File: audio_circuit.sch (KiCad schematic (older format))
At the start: 21 parts

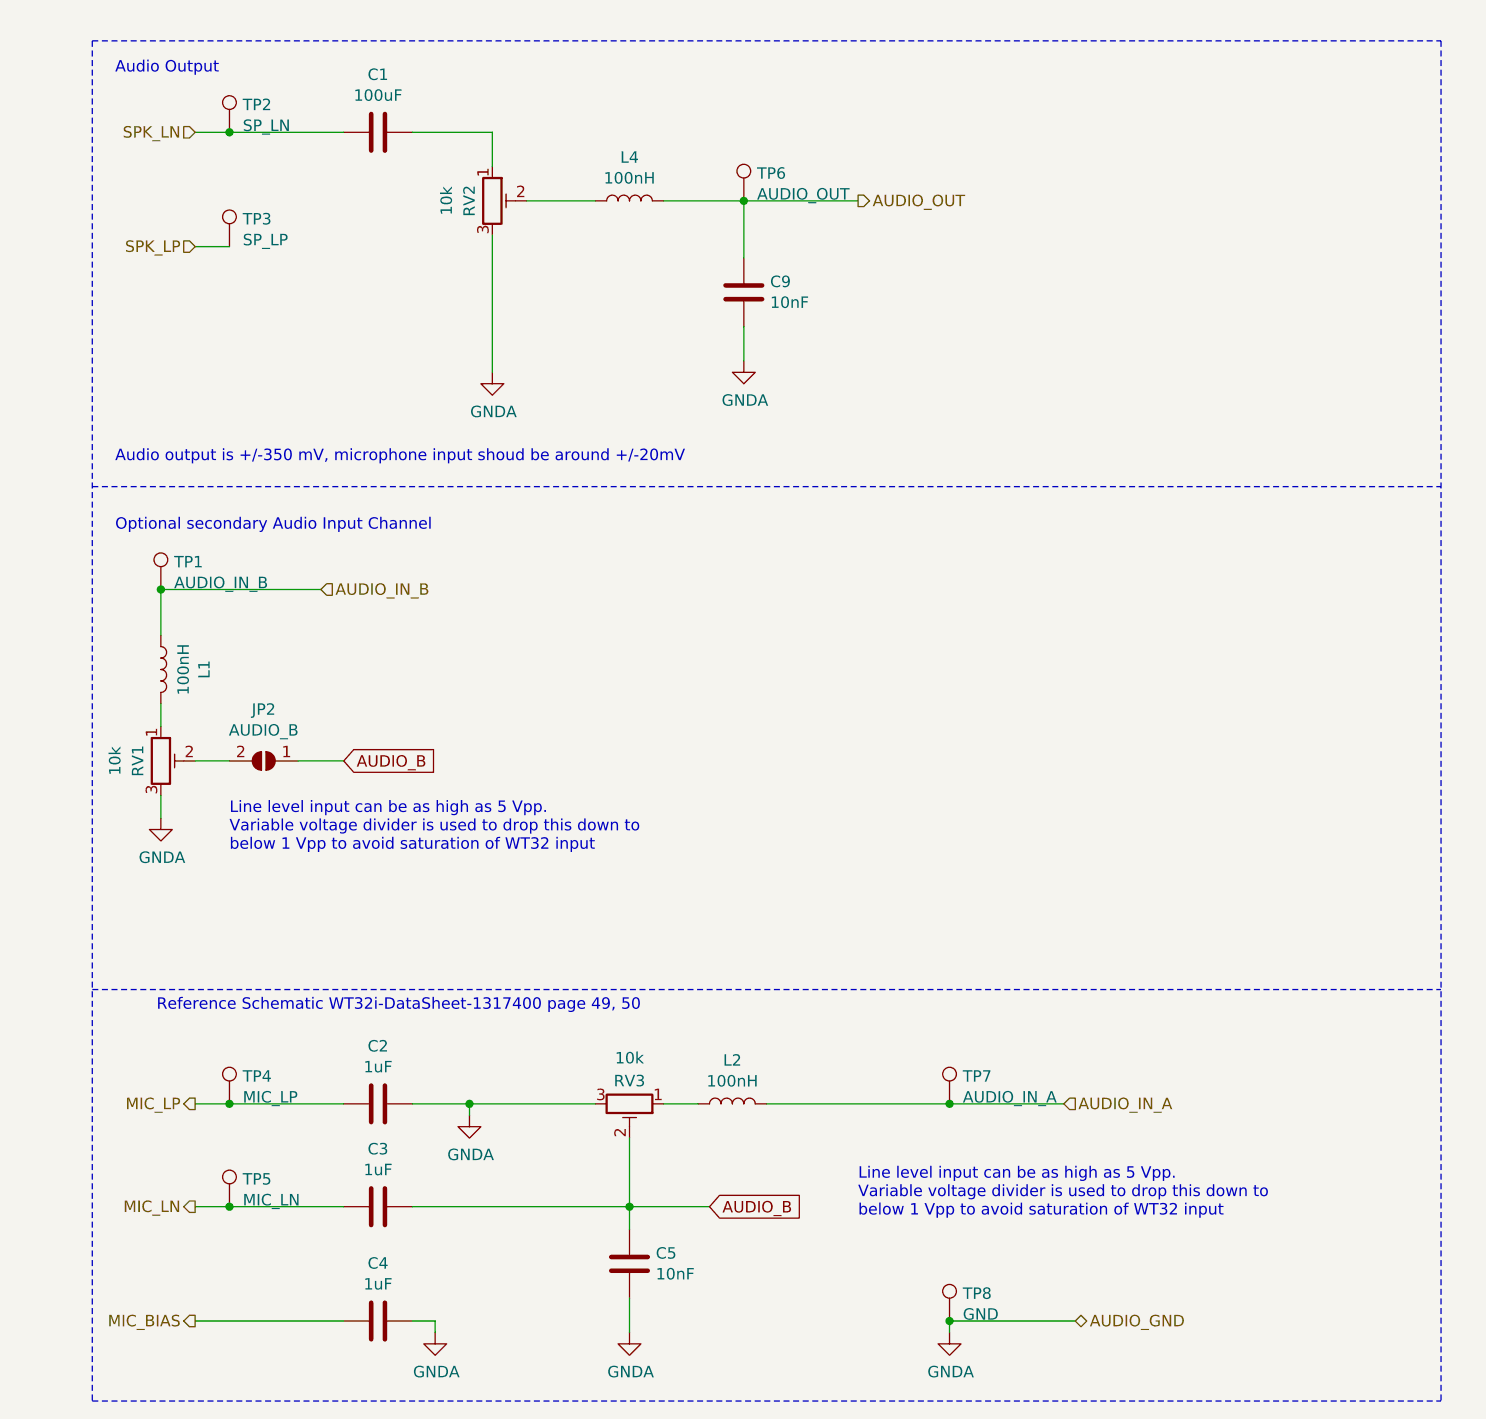
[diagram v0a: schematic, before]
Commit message: Assigned Pins to ESP32 and removed Teensy [#1]
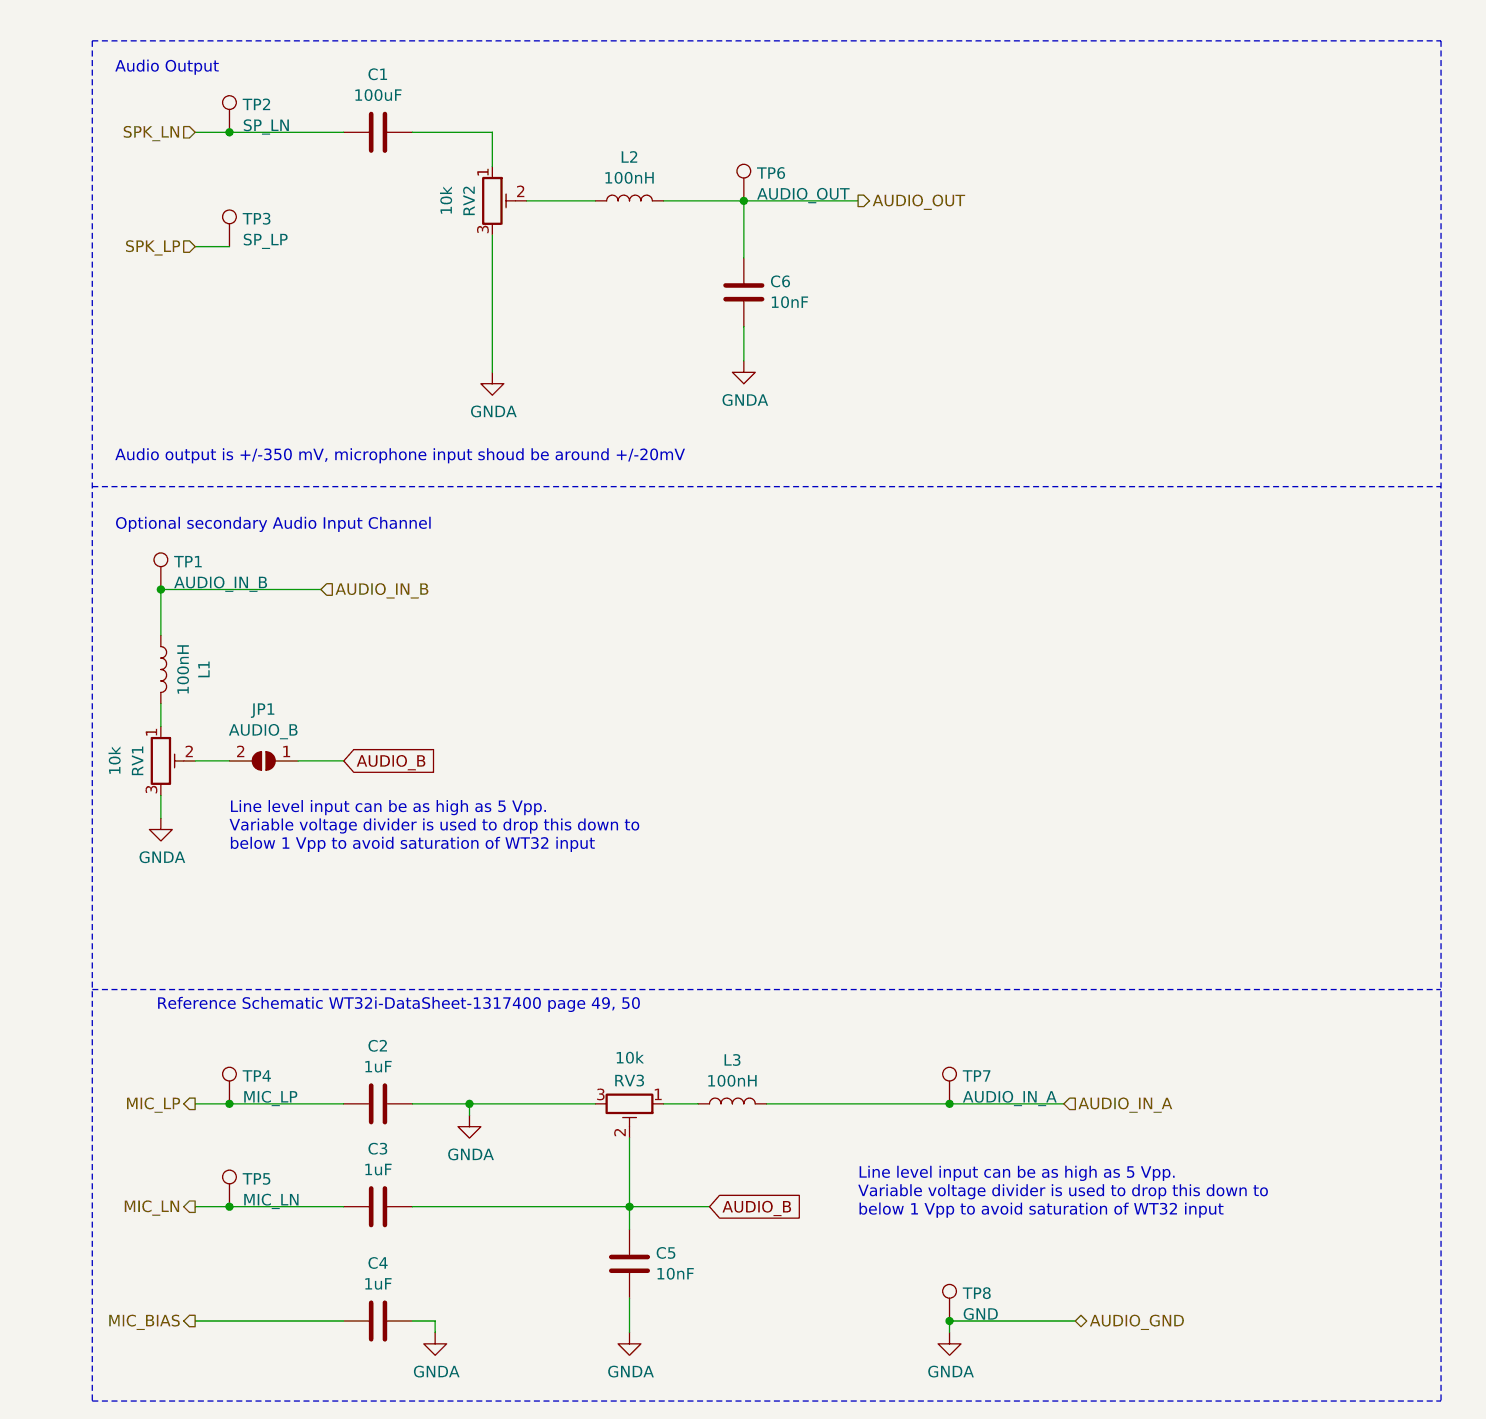
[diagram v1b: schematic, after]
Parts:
- renumbered C9 to C6, JP2 to JP1, L4 to L2, L2 to L3
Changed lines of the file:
@@
 $EndComp
 $Comp
-L power:GNDA #PWR016
+L power:GNDA #PWR015
 U 1 1 5C1B0B4E
 P 2300 6900
-F 0 "#PWR016" H 2300 6650 50  0001 C CNN
+F 0 "#PWR015" H 2300 6650 50  0001 C CNN
 F 1 "GNDA" H 2305 6727 50  0000 C CNN
 F 2 "" H 2300 6900 50  0001 C CNN
@@
 Reference Schematic WT32i-DataSheet-1317400 page 49, 50
 $Comp
-L power:GNDA #PWR019
+L power:GNDA #PWR018
 U 1 1 5C1B2321
 P 3150 6900
-F 0 "#PWR019" H 3150 6650 50  0001 C CNN
+F 0 "#PWR018" H 3150 6650 50  0001 C CNN
 F 1 "GNDA" H 3155 6727 50  0000 C CNN
 F 2 "" H 3150 6900 50  0001 C CNN
@@
 	4550 6900 4550 6850
 $Comp
-L Device:L L2
+L Device:L L3
 U 1 1 5BFC0C35
 P 3600 5900
-F 0 "L2" V 3790 5900 50  0000 C CNN
+F 0 "L3" V 3790 5900 50  0000 C CNN
 F 1 "100nH" V 3699 5900 50  0000 C CNN
 F 2 "Inductor_SMD:L_0805_2012Metric_Pad1.15x1.40mm_HandSolder" H 3600 5900 50  0001 C CNN
@@
 	2450 5900 2450 5950
 $Comp
-L power:GNDA #PWR017
+L power:GNDA #PWR016
 U 1 1 5C1B2304
 P 2450 5950
-F 0 "#PWR017" H 2450 5700 50  0001 C CNN
+F 0 "#PWR016" H 2450 5700 50  0001 C CNN
 F 1 "GNDA" H 2455 5777 50  0000 C CNN
 F 2 "" H 2450 5950 50  0001 C CNN
@@
 $EndComp
 $Comp
-L power:GNDA #PWR015
+L power:GNDA #PWR014
 U 1 1 5C7723EC
 P 1100 4650
-F 0 "#PWR015" H 1100 4400 50  0001 C CNN
+F 0 "#PWR014" H 1100 4400 50  0001 C CNN
 F 1 "GNDA" H 1105 4477 50  0000 C CNN
 F 2 "" H 1100 4650 50  0001 C CNN
@@
 	4550 6850 5100 6850
 $Comp
-L Jumper:SolderJumper_2_Open JP2
+L Jumper:SolderJumper_2_Open JP1
 U 1 1 5C773465
 P 1550 4400
-F 0 "JP2" H 1550 4175 50  0000 C CNN
+F 0 "JP1" H 1550 4175 50  0000 C CNN
 F 1 "AUDIO_B" H 1550 4266 50  0000 C CNN
 F 2 "Jumper:SolderJumper-2_P1.3mm_Open_TrianglePad1.0x1.5mm" H 1550 4400 50  0001 C CNN
@@
 $EndComp
 $Comp
-L power:GNDA #PWR018
+L power:GNDA #PWR017
 U 1 1 5C77530F
 P 2550 2700
-F 0 "#PWR018" H 2550 2450 50  0001 C CNN
+F 0 "#PWR017" H 2550 2450 50  0001 C CNN
 F 1 "GNDA" H 2555 2527 50  0000 C CNN
 F 2 "" H 2550 2700 50  0001 C CNN
@@
 	1250 2150 1400 2150
 $Comp
-L Device:L L4
+L Device:L L2
 U 1 1 5CD0D38F
 P 3150 1950
-F 0 "L4" V 3340 1950 50  0000 C CNN
+F 0 "L2" V 3340 1950 50  0000 C CNN
 F 1 "100nH" V 3249 1950 50  0000 C CNN
 F 2 "Inductor_SMD:L_0805_2012Metric_Pad1.15x1.40mm_HandSolder" H 3150 1950 50  0001 C CNN
@@
 $EndComp
 $Comp
-L power:GNDA #PWR042
+L power:GNDA #PWR019
 U 1 1 5CD0D82A
 P 3650 2650
-F 0 "#PWR042" H 3650 2400 50  0001 C CNN
+F 0 "#PWR019" H 3650 2400 50  0001 C CNN
 F 1 "GNDA" H 3655 2477 50  0000 C CNN
 F 2 "" H 3650 2650 50  0001 C CNN
@@
 $EndComp
 $Comp
-L Device:C C9
+L Device:C C6
 U 1 1 5CD0D832
 P 3650 2350
-F 0 "C9" H 3765 2396 50  0000 L CNN
+F 0 "C6" H 3765 2396 50  0000 L CNN
 F 1 "10nF" H 3765 2305 50  0000 L CNN
 F 2 "Capacitor_SMD:C_0805_2012Metric_Pad1.15x1.40mm_HandSolder" H 3688 2200 50  0001 C CNN
